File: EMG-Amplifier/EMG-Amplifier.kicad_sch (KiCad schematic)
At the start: 18 parts, among them U1 AD623, U2 LM741, U3 LM741, U4 LM741, U5 Amp

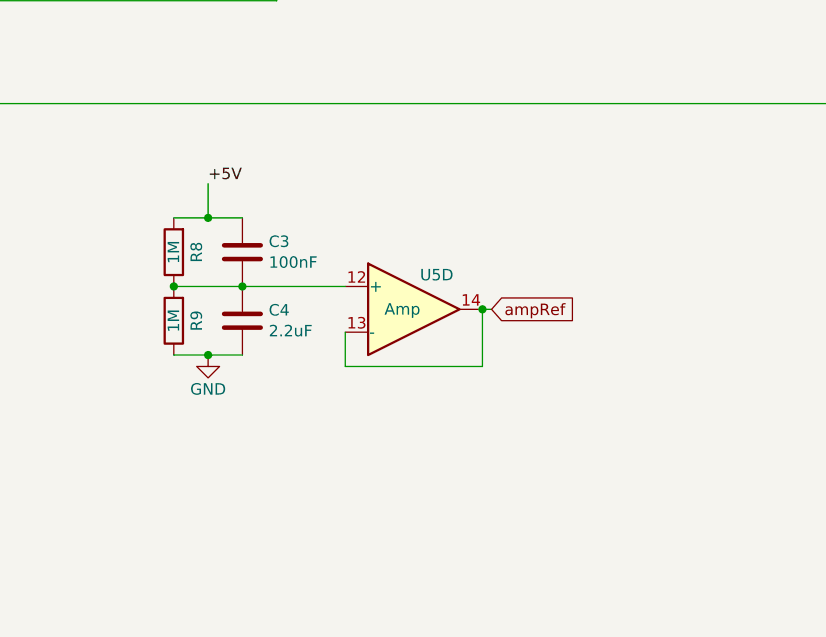
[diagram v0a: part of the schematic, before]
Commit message: Updated the schematic to use LM741 instead of LM324
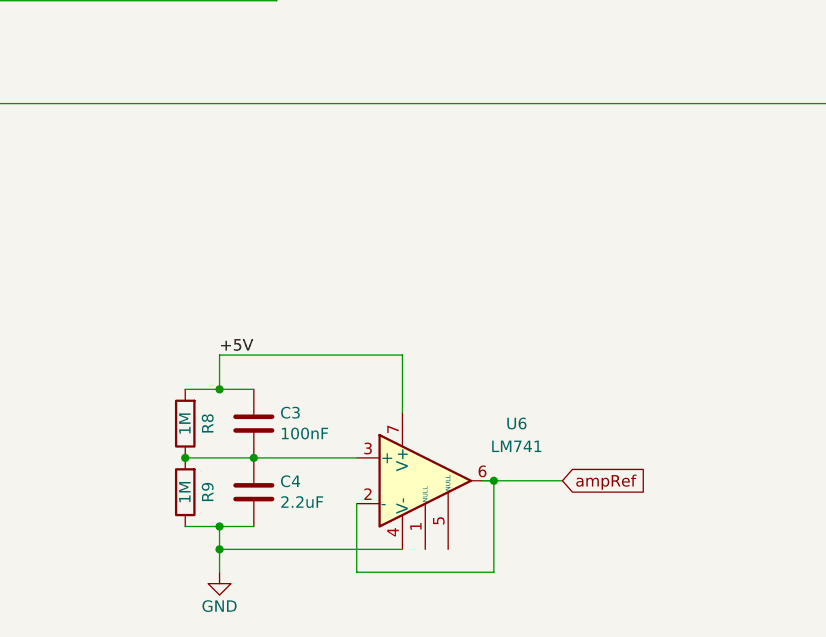
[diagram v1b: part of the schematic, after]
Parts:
- removed U5: Amp, Package_SO:SOIC-14_3.9x8.7mm_P1.27mm, symbol Amplifier_Operational:LM324
- added U6: LM741, symbol Amplifier_Operational:LM741
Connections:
- net +5V: now also U6.7 (V+)
- net GND: now also U6.4 (V-)
- net ampRef: now also U6.2 (-), U6.6
- net at C3.1, C4.2, R8.1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: now also U6.3 (+)
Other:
- moved on the sheet: C3, C4, R8, R9

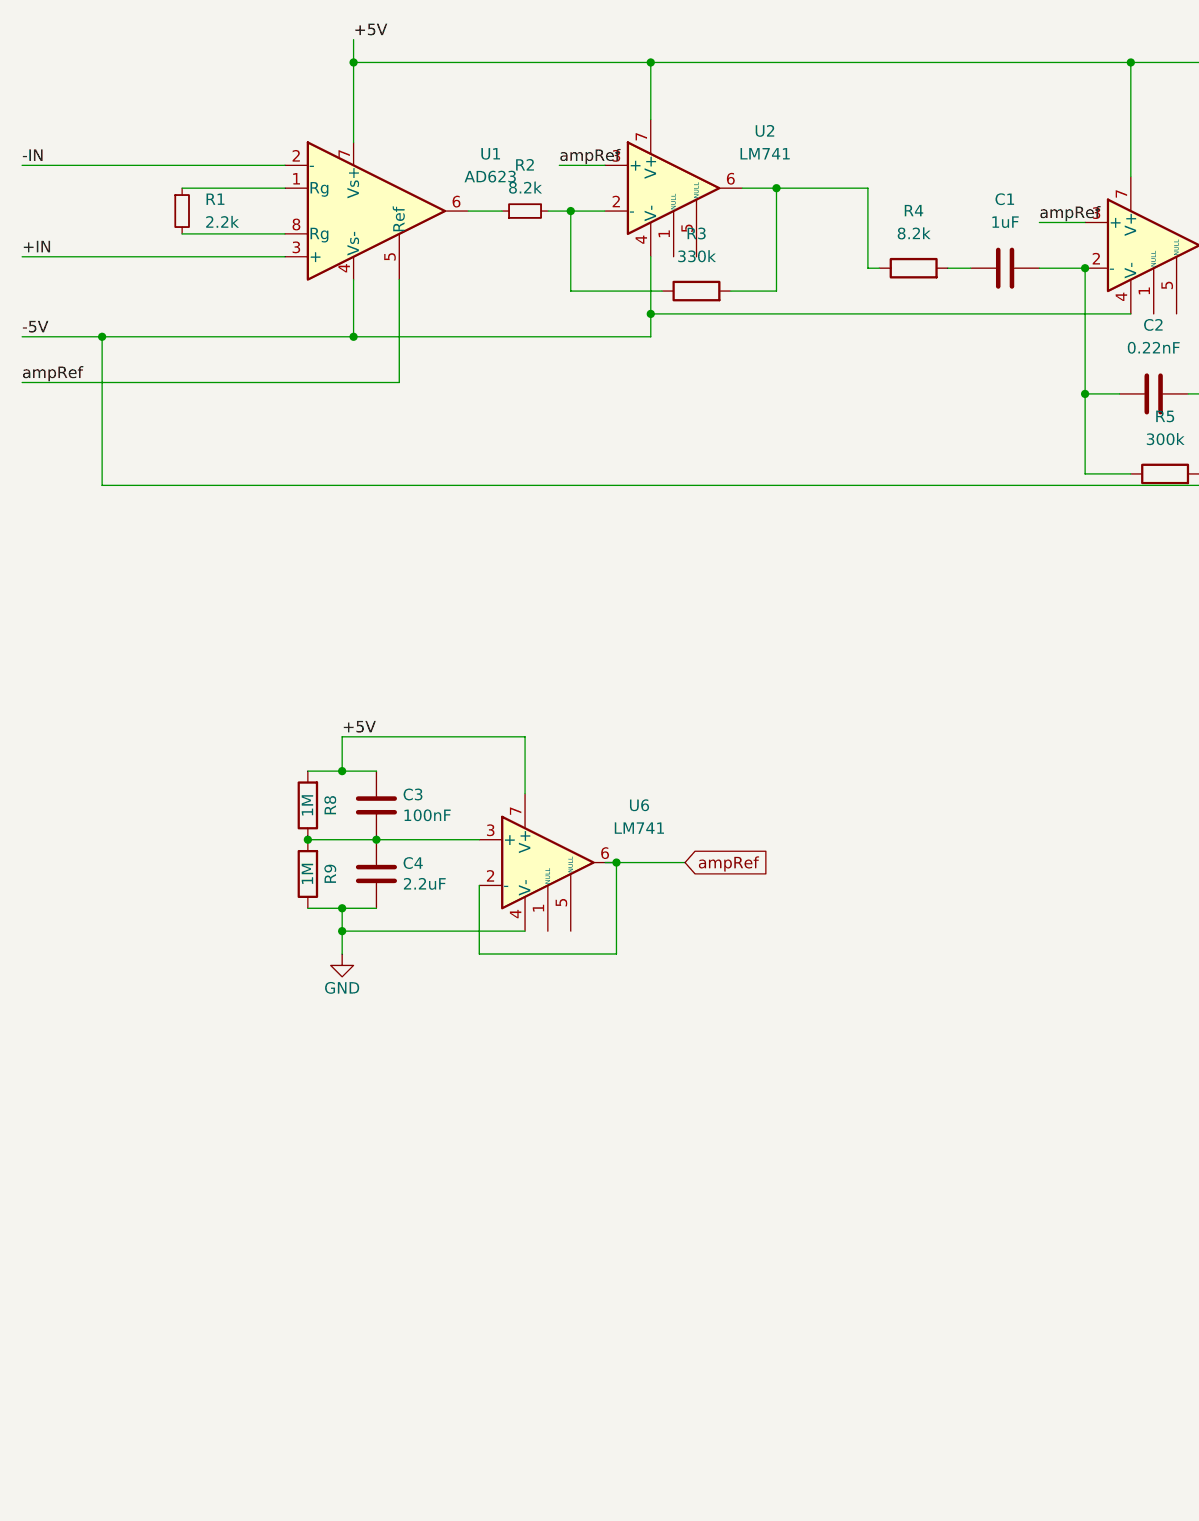
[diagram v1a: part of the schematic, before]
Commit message: Added the AD623 equivalent circuit
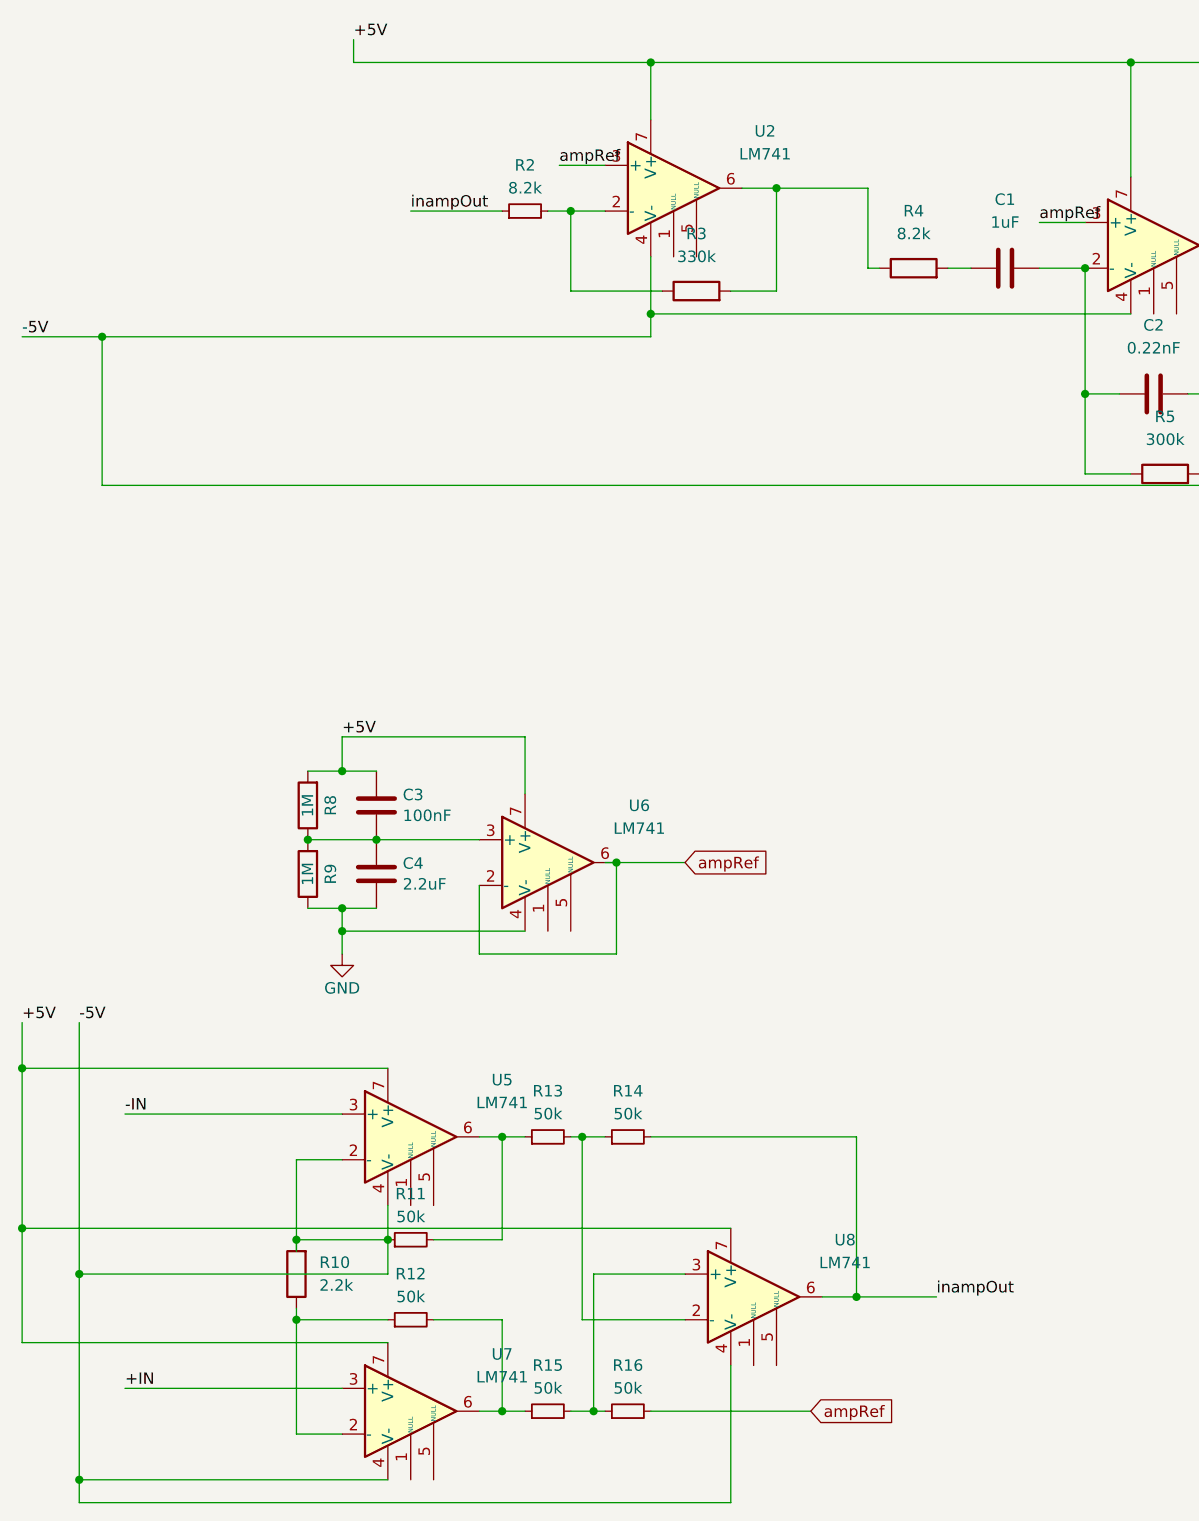
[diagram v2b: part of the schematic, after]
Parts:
- removed R1: 2.2k, symbol Device:R_Small
- removed U1: AD623, symbol Amplifier_Instrumentation:AD623
- added R10: 2.2k, symbol Device:R
- added R11, R12, R13, R14, R15, R16: 50k, symbol Device:R_Small
- added U5, U7, U8: LM741, symbol Amplifier_Operational:LM741
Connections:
- net +5V: now also U5.7 (V+), U7.7 (V+), U8.7 (V+)
- net +IN: now also U7.3 (+)
- net -5V: now also R10.2, R11.1, U5.2 (-), U5.4 (V-), U7.4 (V-), U8.4 (V-)
- net -IN : now also U5.3 (+)
- net ampRef: now also R16.2
- net inampOut: now reaches R2.1
- net inampOut: now also R14.2, U8.6
- new net: R10.1, R12.1, U7.2 (-)
- new net: R12.2, R15.1, U7.6
- new net: R11.2, R13.1, U5.6
- new net: R15.2, R16.1, U8.3 (+)
- new net: R13.2, R14.1, U8.2 (-)

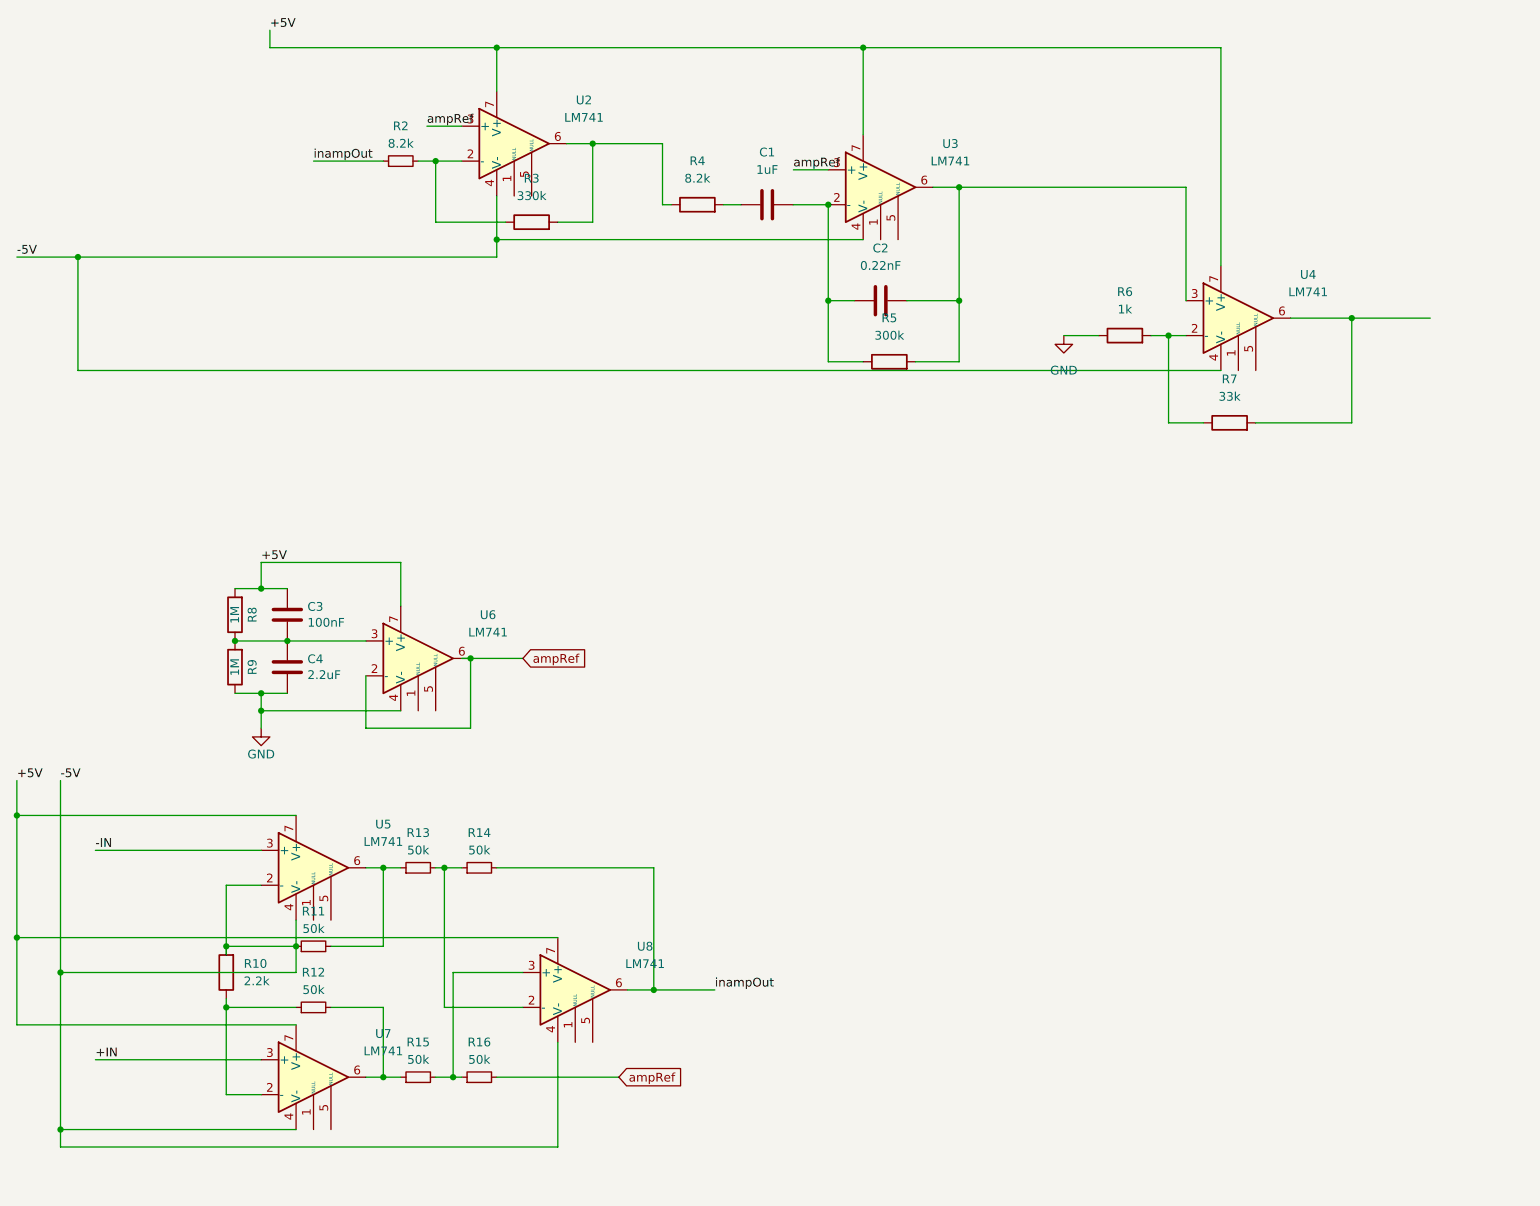
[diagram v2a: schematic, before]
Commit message: Mentioned gain for circuit
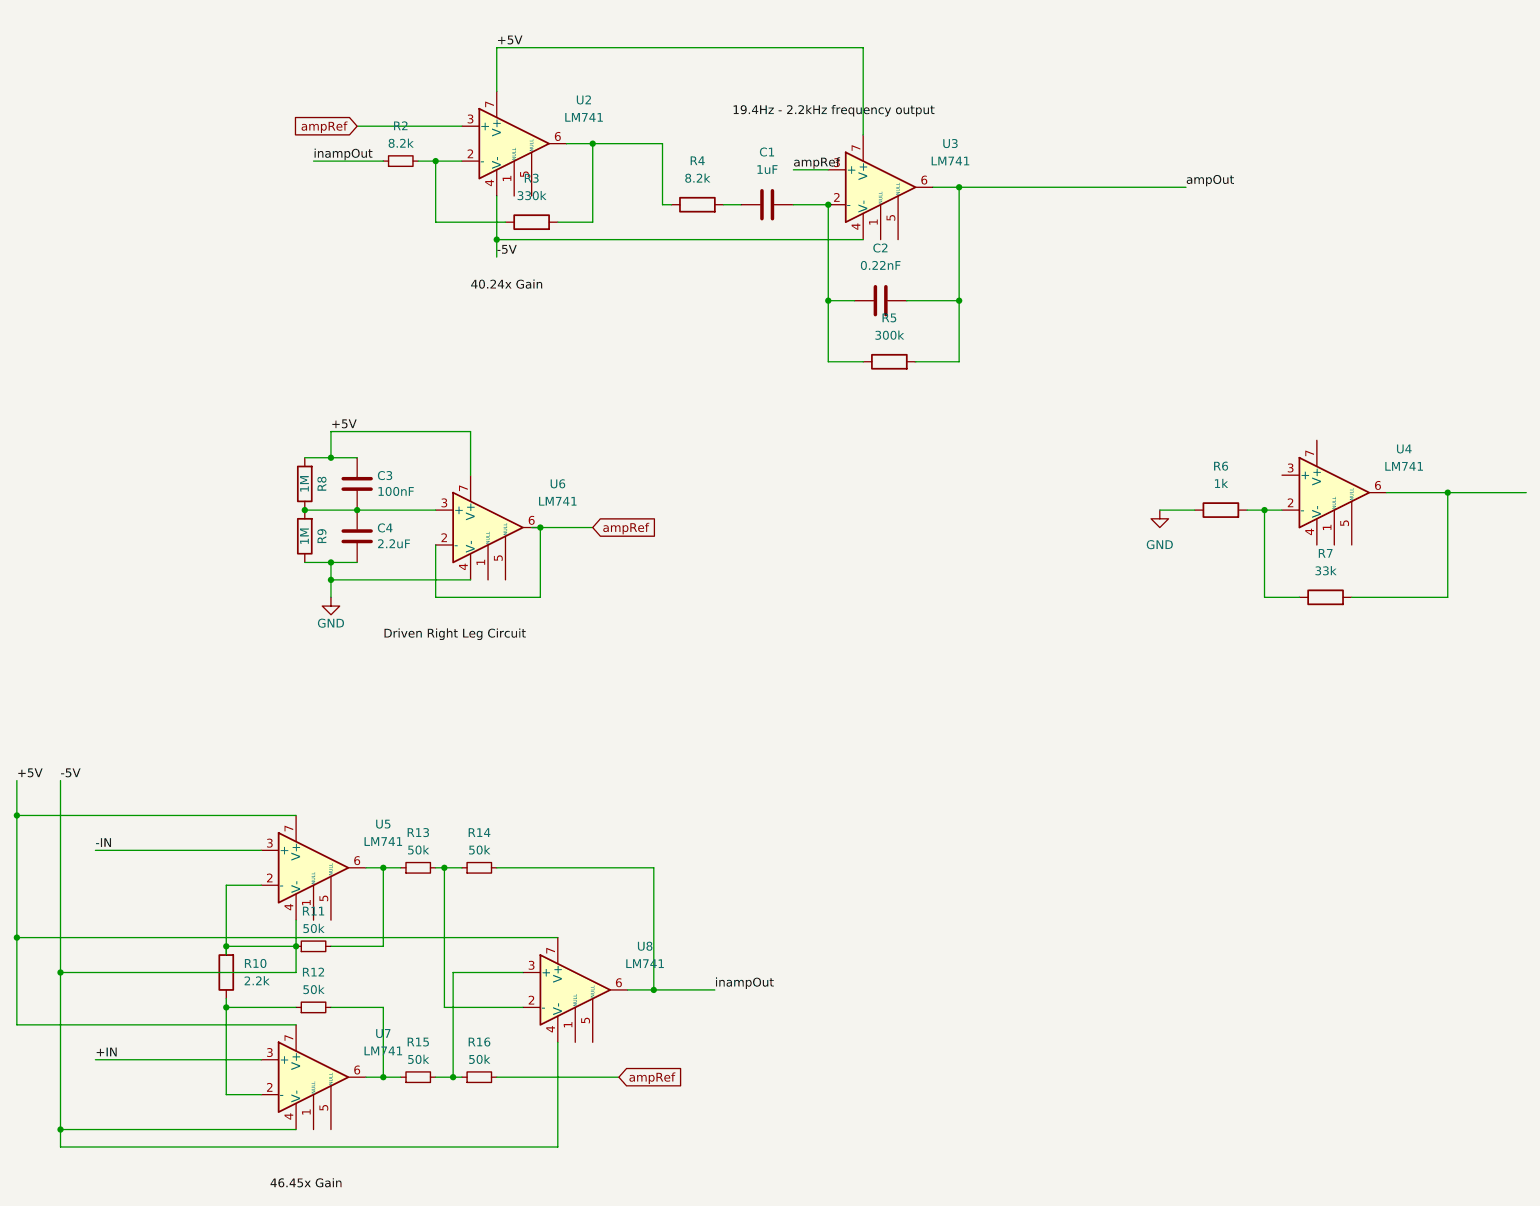
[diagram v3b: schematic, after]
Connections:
- net +5V: no longer U4.7 (V+)
- net -5V: no longer U4.4 (V-)
- net ampOut: now reaches C2.1, R5.2, U3.6
- net ampOut: no longer U4.3 (+)
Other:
- moved on the sheet: C3, C4, R6, R7, R8, R9, U4, U6

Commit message: Added the bill of materials csv
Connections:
- net +5V is gone; now on net GND: C3.2, R8.2, U2.7 (V+), U3.7 (V+), U5.7 (V+), U6.7 (V+), U7.7 (V+), U8.7 (V+)
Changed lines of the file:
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@@
+	)
+	(junction
+		(at 74.93 85.09)
+		(diameter 0)
+		(color 0 0 0 0)
 	)
 	(junction
@@
 	)
 	(junction
+		(at 99.06 102.87)
+		(diameter 0)
+		(color 0 0 0 0)
+	)
+	(junction
 		(at 86.36 144.78)
 		(diameter 0)
@@
 	)
 	(junction
-		(at 78.74 85.09)
-		(diameter 0)
-		(color 0 0 0 0)
-	)
-	(junction
 		(at 63.5 165.1)
 		(diameter 0)
@@
 	(wire
 		(pts
-			(xy 99.06 81.28) (xy 78.74 81.28)
+			(xy 99.06 440.69) (xy -426.72 440.69)
 		)
 		(stroke
@@
 	(wire
 		(pts
+			(xy 74.93 85.09) (xy 82.55 85.09)
+		)
+		(stroke
+			(width 0)
+			(type default)
+		)
+	)
+	(wire
+		(pts
 			(xy 93.98 175.26) (xy 96.52 175.26)
 		)
@@
 	(wire
 		(pts
-			(xy 99.06 87.63) (xy 99.06 81.28)
+			(xy 99.06 87.63) (xy 99.06 102.87)
 		)
 		(stroke
@@
 	(wire
 		(pts
-			(xy 78.74 81.28) (xy 78.74 85.09)
+			(xy -426.72 440.69) (xy -426.72 85.09)
 		)
 		(stroke
@@
 	(wire
 		(pts
-			(xy 78.74 85.09) (xy 82.55 85.09)
-		)
-		(stroke
-			(width 0)
-			(type default)
-		)
-	)
-	(wire
-		(pts
 			(xy 104.14 50.8) (xy 93.98 50.8)
 		)
@@
 	(wire
 		(pts
+			(xy 99.06 102.87) (xy 99.06 440.69)
+		)
+		(stroke
+			(width 0)
+			(type default)
+		)
+	)
+	(wire
+		(pts
 			(xy 162.56 62.23) (xy 170.18 62.23)
 		)
@@
 	(wire
 		(pts
-			(xy 74.93 85.09) (xy 78.74 85.09)
-		)
-		(stroke
-			(width 0)
-			(type default)
-		)
-	)
-	(wire
-		(pts
 			(xy 33.02 132.08) (xy 33.02 137.16)
 		)
@@
 		(pts
 			(xy 127 39.37) (xy 127 48.26)
+		)
+		(stroke
+			(width 0)
+			(type default)
+		)
+	)
+	(wire
+		(pts
+			(xy -426.72 85.09) (xy 74.93 85.09)
 		)
 		(stroke
@@
 	)
 	(label "+5V"
-		(at 78.74 81.28 0)
-		(fields_autoplaced yes)
-		(effects
+		(at 78.74 440.69 0)
+		(fields_autoplaced yes)
+		(effects

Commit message: Changed schematic for LM324
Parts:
- removed U5, U6, U7, U8: LM741, symbol Amplifier_Operational:LM741
- added C5, C7: 100pF, Capacitor_SMD:C_0805_2012Metric_Pad1.18x1.45mm_HandSolder, symbol Device:C
- added C6: 1nF, Capacitor_SMD:C_0805_2012Metric_Pad1.18x1.45mm_HandSolder, symbol Device:C
- added R1, R17: 1K, Resistor_SMD:R_0805_2012Metric_Pad1.20x1.40mm_HandSolder, symbol Device:R
- added U1, U9: LM324, symbol Amplifier_Operational:LM324
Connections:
- net +IN: now also C6.1, C7.2, R17.1, U1.5 (+)
- net -5V: no longer R10.2, R11.1
- net -IN : now also C5.1, C6.2, R1.1, U9.3 (+)
- net GND: now also U1.11 (V-); no longer C3.2, R8.2, U2.7 (V+), U3.7 (V+)
- net ampRef: now also C5.2, C7.1, U1.13 (-), U1.14
- net inampOut: now also U1.8
- net at R10.1, R12.1: now also U1.6 (-)
- net at R12.2, R15.1: now also U1.7
- net at C3.1, C4.2, R8.1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: now also U1.12 (+)
- net at R11.2, R13.1: now also U9.1
- net at R15.2, R16.1: now also U1.10 (+)
- net at R13.2, R14.1: now also U1.9 (-)
- new net: R10.2, R11.1, U9.2 (-)
- new net +5V: C3.2, R8.2, U1.4 (V+), U2.7 (V+), U3.7 (V+)
- new net bioIN+: R17.2
- new net bioIN-: R1.2
